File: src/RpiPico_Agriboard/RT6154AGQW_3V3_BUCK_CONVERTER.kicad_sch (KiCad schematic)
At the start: 14 parts, among them U1 RT6154A/B

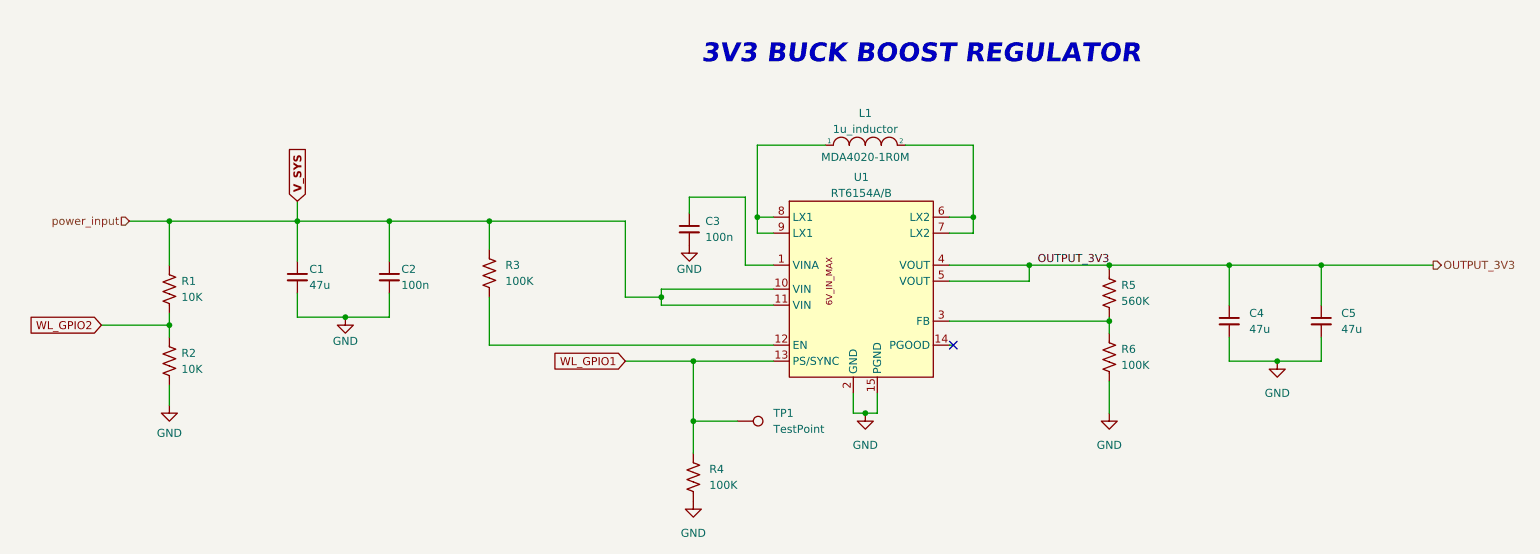
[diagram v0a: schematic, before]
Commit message: complete board update and routing
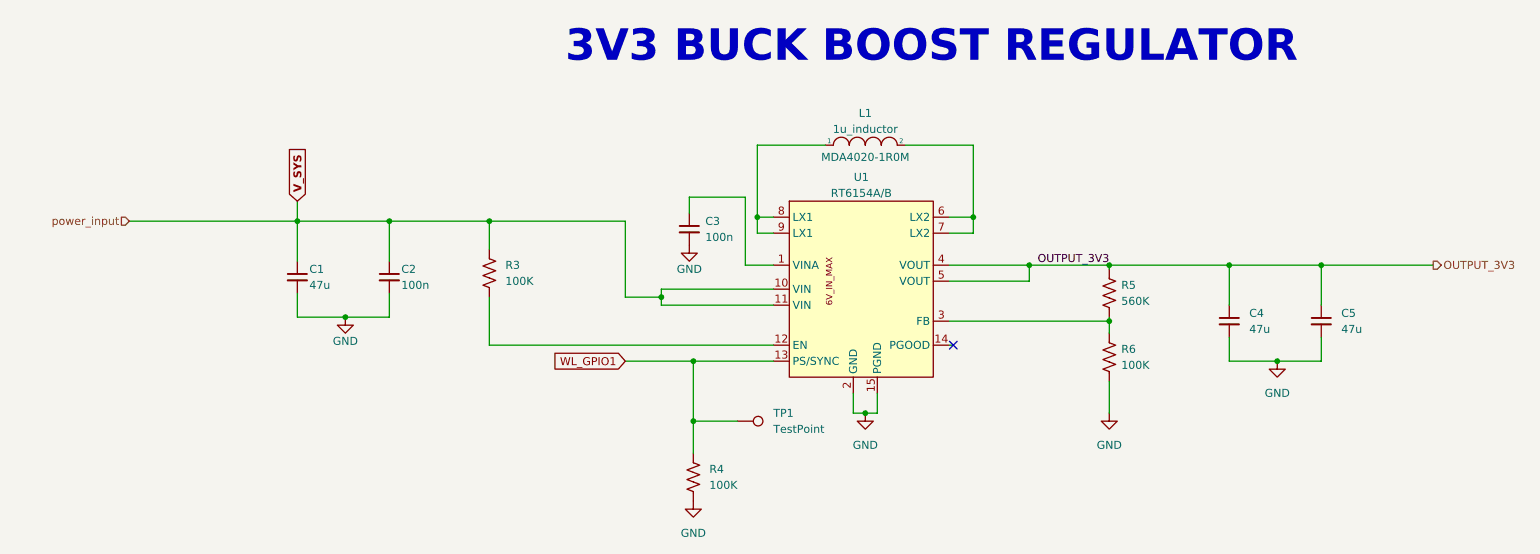
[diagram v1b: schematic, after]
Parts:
- removed R1, R2: 10K, Resistor_SMD:R_0402_1005Metric, symbol Device:R_US
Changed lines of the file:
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@@
   (junction (at 73.025 75.565) (diameter 0) (color 0 0 0 0)
   )
-  (junction (at 52.705 75.565) (diameter 0) (color 0 0 0 0)
-  )
   (junction (at 235.585 82.55) (diameter 0) (color 0 0 0 0)
   )
@@
   )
   (junction (at 180.34 74.93) (diameter 0) (color 0 0 0 0)
-  )
-  (junction (at 52.705 92.075) (diameter 0) (color 0 0 0 0)
   )
   (junction (at 80.645 90.805) (diameter 0) (color 0 0 0 0)
@@
     (stroke (width 0) (type default))
   )
-  (wire (pts (xy 52.705 101.6) (xy 52.705 104.775))
-    (stroke (width 0) (type default))
-  )
   (wire (pts (xy 220.98 88.9) (xy 220.98 82.55))
     (stroke (width 0) (type default))
@@
     (stroke (width 0) (type default))
   )
-  (wire (pts (xy 52.705 75.565) (xy 52.705 82.55))
-    (stroke (width 0) (type default))
-  )
   (wire (pts (xy 87.63 75.565) (xy 87.63 81.915))
     (stroke (width 0) (type default))
@@
     (stroke (width 0) (type default))
   )
-  (wire (pts (xy 52.705 75.565) (xy 73.025 75.565))
+  (wire (pts (xy 46.355 75.565) (xy 73.025 75.565))
     (stroke (width 0) (type default))
   )
@@
     (stroke (width 0) (type default))
   )
-  (wire (pts (xy 46.355 75.565) (xy 52.705 75.565))
-    (stroke (width 0) (type default))
-  )
   (wire (pts (xy 135.89 107.315) (xy 135.89 112.395))
     (stroke (width 0) (type default))
@@
     (stroke (width 0) (type default))
   )
-  (wire (pts (xy 41.91 92.075) (xy 52.705 92.075))
-    (stroke (width 0) (type default))
-  )
   (wire (pts (xy 135.89 107.315) (xy 142.875 107.315))
     (stroke (width 0) (type default))
@@
     (stroke (width 0) (type default))
   )
-  (wire (pts (xy 52.705 92.075) (xy 52.705 93.98))
-    (stroke (width 0) (type default))
-  )
   (wire (pts (xy 130.81 87.63) (xy 125.095 87.63))
     (stroke (width 0) (type default))
@@
     (stroke (width 0) (type default))
   )
-  (wire (pts (xy 52.705 90.17) (xy 52.705 92.075))
-    (stroke (width 0) (type default))
-  )
   (wire (pts (xy 148.59 86.36) (xy 130.81 86.36))
     (stroke (width 0) (type default))
@@
     (stroke (width 0) (type default))
   )
-  (text "3V3 BUCK BOOST REGULATOR" (at 137.16 50.8 0)
-    (effects (font (size 3 3) bold italic) (justify left bottom))
+  (text "3V3 BUCK BOOST REGULATOR" (at 115.57 50.8 0)
+    (effects (font (face "Agency FB") (size 5 5) bold) (justify left bottom))
   )
   (label "OUTPUT_3V3" (at 201.93 82.55 180) (fields_autoplaced)
@@
     )
   )
-  (global_label "WL_GPIO2" (shape input) (at 41.91 92.075 180) (fields_autoplaced)
-    (effects (font (size 1.27 1.27)) (justify right))
-    (property "Intersheetrefs" "${INTERSHEET_REFS}" (at 30.365 91.9956 0)
-      (effects (font (size 1.27 1.27)) (justify right) hide)
-    )
-  )
   (global_label "V_SYS" (shape input) (at 73.025 72.39 90) (fields_autoplaced)
     (effects (font (size 1.27 1.27) bold) (justify left))
@@
     )
   )
-  (symbol (lib_id "Device:R_US") (at 52.705 86.36 0) (unit 1)
-    (in_bom yes) (on_board yes) (dnp no) (fields_autoplaced)
-    (property "Reference" "R1" (at 54.61 85.0899 0)
-      (effects (font (size 1.27 1.27)) (justify left))
-    )
-    (property "Value" "10K" (at 54.61 87.6299 0)
-      (effects (font (size 1.27 1.27)) (justify left))
-    )
-    (property "Footprint" "Resistor_SMD:R_0402_1005Metric" (at 53.721 86.614 90)
-      (effects (font (size 1.27 1.27)) hide)
-    )
-    (property "Datasheet" "~" (at 52.705 86.36 0)
-      (effects (font (size 1.27 1.27)) hide)
-    )
-    (pin "1")
-    (pin "2")
-    (instances
-      (project "RpiPico_Agriboard"
-        (path "/c2474b65-c0e8-4987-86b2-fddddd4113dc/cfc0dd9f-3180-4dac-a3f9-f91bbb704852"
-          (reference "R1") (unit 1)
-        )
-      )
-    )
-  )
   (symbol (lib_id "Device:C_Small") (at 135.255 76.835 0) (unit 1)
     (in_bom yes) (on_board yes) (dnp no) (fields_autoplaced)
@@
     )
   )
-  (symbol (lib_id "power:GND") (at 52.705 104.775 0) (unit 1)
-    (in_bom yes) (on_board yes) (dnp no) (fields_autoplaced)
-    (property "Reference" "#PWR02" (at 52.705 111.125 0)
-      (effects (font (size 1.27 1.27)) hide)
-    )
-    (property "Value" "GND" (at 52.705 109.22 0)
-      (effects (font (size 1.27 1.27)))
-    )
-    (property "Footprint" "" (at 52.705 104.775 0)
-      (effects (font (size 1.27 1.27)) hide)
-    )
-    (property "Datasheet" "" (at 52.705 104.775 0)
-      (effects (font (size 1.27 1.27)) hide)
-    )
-    (pin "1")
-    (instances
-      (project "RpiPico_Agriboard"
-        (path "/c2474b65-c0e8-4987-86b2-fddddd4113dc/cfc0dd9f-3180-4dac-a3f9-f91bbb704852"
-          (reference "#PWR02") (unit 1)
-        )
-      )
-    )
-  )
   (symbol (lib_id "Device:C_Small") (at 87.63 84.455 0) (unit 1)
     (in_bom yes) (on_board yes) (dnp no)
@@
         )
       )
-    )
-  )
-  (symbol (lib_id "Device:R_US") (at 52.705 97.79 0) (unit 1)
-    (in_bom yes) (on_board yes) (dnp no) (fields_autoplaced)
-    (property "Reference" "R2" (at 54.61 96.5199 0)
-      (effects (font (size 1.27 1.27)) (justify left))
-    )
-    (property "Value" "10K" (at 54.61 99.0599 0)
-      (effects (font (size 1.27 1.27)) (justify left))
-    )
-    (property "Footprint" "Resistor_SMD:R_0402_1005Metric" (at 53.721 98.044 90)
-      (effects (font (size 1.27 1.27)) hide)
-    )
-    (property "Datasheet" "~" (at 52.705 97.79 0)
-      (effects (font (size 1.27 1.27)) hide)
-    )
-    (pin "1")
-    (pin "2")
-    (instances
-      (project "RpiPico_Agriboard"
-        (path "/c2474b65-c0e8-4987-86b2-fddddd4113dc/cfc0dd9f-3180-4dac-a3f9-f91bbb704852"
-          (reference "R2") (unit 1)
-        )
-      )
